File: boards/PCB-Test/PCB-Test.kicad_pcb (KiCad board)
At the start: 2 copper layers, 35.6 x 50.8 mm, 5 parts, among them U1 74HC137, U2 74HC137, U3 74HC137, U4 ATmega32-16A, U5 ATmega32-16M

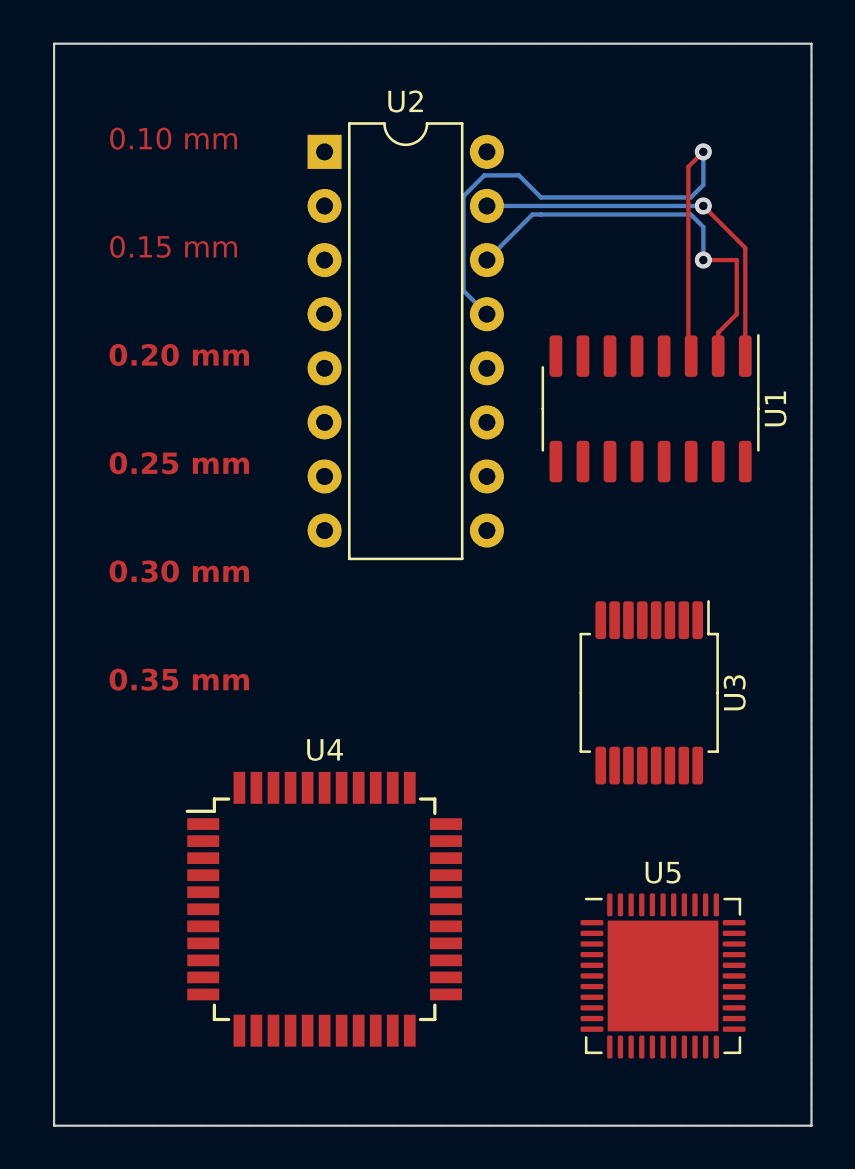
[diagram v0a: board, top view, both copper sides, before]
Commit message: Update PCB test board with different track sizes
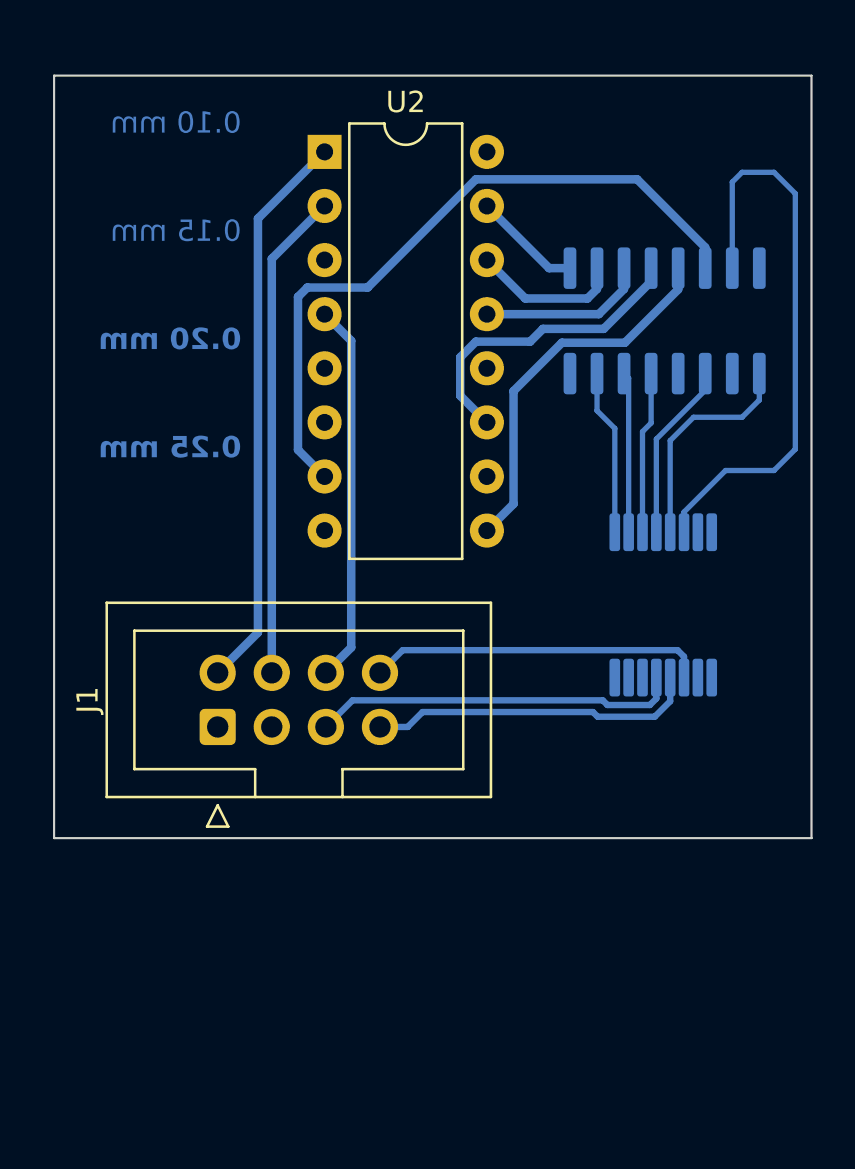
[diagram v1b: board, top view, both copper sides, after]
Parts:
- removed U4: ATmega32-16A, Package_QFP:TQFP-44_10x10mm_P0.8mm
- removed U5: ATmega32-16M, Package_DFN_QFN:QFN-44-1EP_7x7mm_P0.5mm_EP5.2x5.2mm
- added J1: Conn_02x04_Odd_Even, Connector_IDC:IDC-Header_2x04_P2.54mm_Vertical, F.Cu at (83.9, 93.0)
- U1, U3: moved to B.Cu
- moved U1 4.18 mm to (104.9, 74.0)
- moved U3 4.18 mm to (104.8, 87.3)
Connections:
- U2 pad 1: unconnected-(U2-A0-Pad1) -> Net-(J1-Pin_2)
- U2 pad 2: unconnected-(U2-A1-Pad2) -> Net-(J1-Pin_4)
- U2 pad 4: unconnected-(U2-~{LE}-Pad4) -> Net-(J1-Pin_6)
- U3 pad 11: unconnected-(U3-~{Y4}-Pad11) -> Net-(J1-Pin_8)
- U3 pad 12: unconnected-(U3-~{Y3}-Pad12) -> Net-(J1-Pin_7)
- U3 pad 13: unconnected-(U3-~{Y2}-Pad13) -> Net-(J1-Pin_5)
- U3 pad 14: unconnected-(U3-~{Y1}-Pad14) -> Net-(J1-Pin_3)
- U3 pad 15: unconnected-(U3-~{Y0}-Pad15) -> Net-(J1-Pin_1)
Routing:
- net Net-(U1-E2): track 0.00 -> 32.7 mm
- net Net-(U1-~{Y7}): track 0.00 -> 27.0 mm
- net Net-(J1-Pin_2): track 0.00 -> 26.5 mm
- net Net-(J1-Pin_4): track 0.00 -> 22.9 mm
- net Net-(U1-A2): track 29.8 -> 7.91 mm, vias 1 -> 0
- net Net-(J1-Pin_6): track 0.00 -> 17.9 mm
- net Net-(U1-~{E1}): track 0.00 -> 17.8 mm
- net Net-(J1-Pin_5): track 0.00 -> 17.2 mm
- net Net-(J1-Pin_8): track 0.00 -> 15.8 mm
- net Net-(J1-Pin_7): track 0.00 -> 15.4 mm
- net Net-(U1-~{LE}): track 0.00 -> 14.6 mm
- net Net-(U1-A0): track 18.0 -> 5.11 mm, vias 1 -> 0
- net Net-(U1-A1): track 19.3 -> 7.08 mm, vias 1 -> 0
- net Net-(U1-~{Y6}): track 0.00 -> 10.5 mm
- net Net-(U1-~{Y4}): track 0.00 -> 8.40 mm
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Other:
- board size 35.6 x 50.8 mm -> 35.6 x 35.8 mm
- board text removed: "0.30 mm"
- board text removed: "0.35 mm"

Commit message: Updated test PCB for milling, remove too small footprint
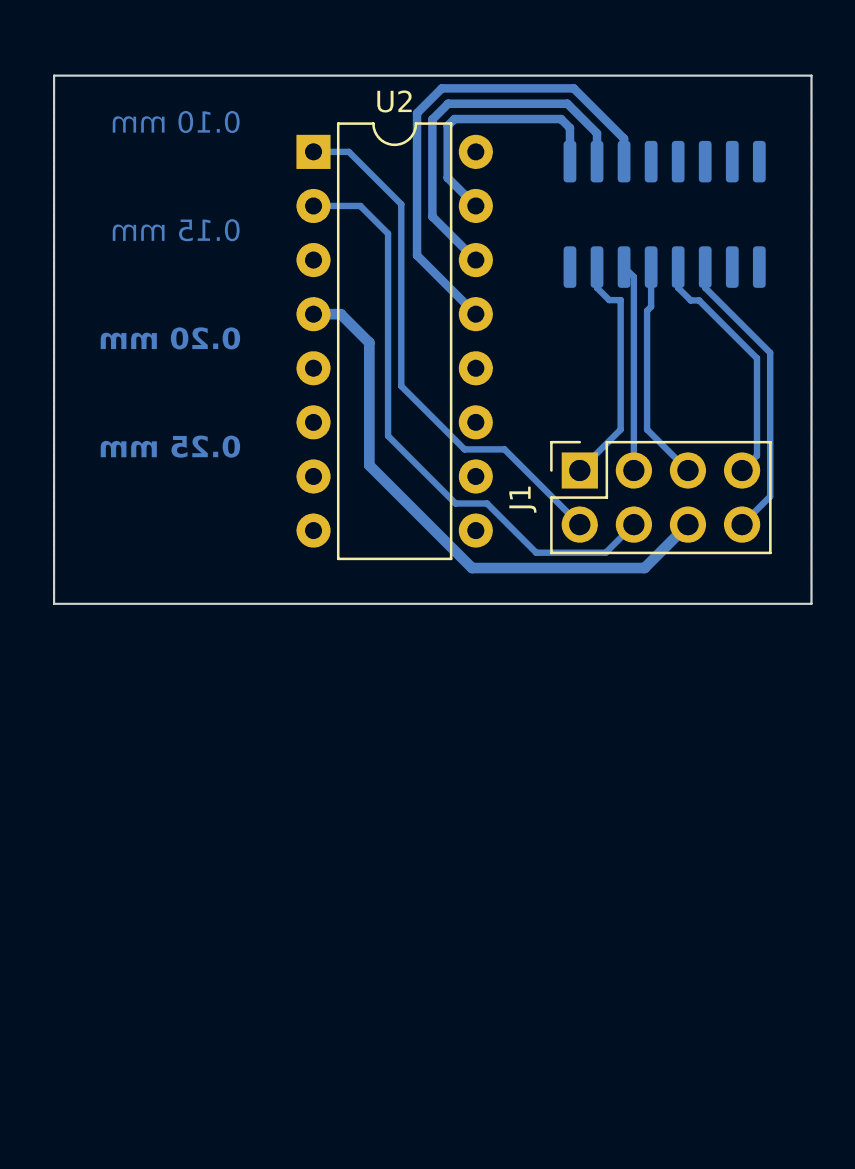
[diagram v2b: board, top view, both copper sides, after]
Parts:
- removed U3: 74HC137, Package_SO:SSOP-16_5.3x6.2mm_P0.65mm
- J1: value Conn_02x04_Odd_Even -> Conn; footprint Connector_IDC:IDC-Header_2x04_P2.54mm_Vertical -> Connector_PinSocket_2.54mm:PinSocket_2x04_P2.54mm_Vertical
- moved J1 20.8 mm to (100.9, 81.0)
- moved U1 5.00 mm to (104.9, 69.0)
- moved U2 0.52 mm to (88.4, 66.0)
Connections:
- U1 pad 11: Net-(U1-~{Y4}) -> Net-(J1-Pin_8)
- U1 pad 12: unconnected-(U1-~{Y3}-Pad12) -> Net-(J1-Pin_7)
- U1 pad 13: Net-(U1-~{Y2}) -> Net-(J1-Pin_5)
- U1 pad 14: Net-(U1-~{Y1}) -> Net-(J1-Pin_3)
- U1 pad 15: Net-(U1-~{Y0}) -> Net-(J1-Pin_1)
- U1 pad 7: Net-(U1-~{Y7}) -> unconnected-(U1-~{Y7}-Pad7)
- U1 pad 9: Net-(U1-~{Y6}) -> unconnected-(U1-~{Y6}-Pad9)
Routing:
- net Net-(U1-E2): track 32.7 -> 0.00 mm
- net Net-(U1-~{Y7}): track 27.0 -> 0.00 mm
- net Net-(U1-~{E1}): track 17.8 -> 0.00 mm
- net Net-(U1-A2): track 7.91 -> 23.6 mm
- net Net-(U1-~{LE}): track 14.6 -> 0.00 mm
- net Net-(J1-Pin_1): track 0.00 -> 11.1 mm
- net Net-(U1-~{Y6}): track 10.5 -> 0.00 mm
- net Net-(U1-A1): track 7.08 -> 17.4 mm
- net Net-(J1-Pin_3): track 0.00 -> 9.74 mm
- net Net-(J1-Pin_6): track 17.9 -> 26.7 mm
- net Net-(U1-~{Y4}): track 8.40 -> 0.00 mm
- net Net-(U1-~{Y0}): track 7.79 -> 0.00 mm
- net Net-(U1-~{Y2}): track 7.62 -> 0.00 mm
- net Net-(U1-~{Y1}): track 7.54 -> 0.00 mm
- net Net-(U1-A0): track 5.11 -> 11.9 mm
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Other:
- board size 35.6 x 35.8 mm -> 35.6 x 24.8 mm

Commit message: Added new PCB design rule templates for PCB milling
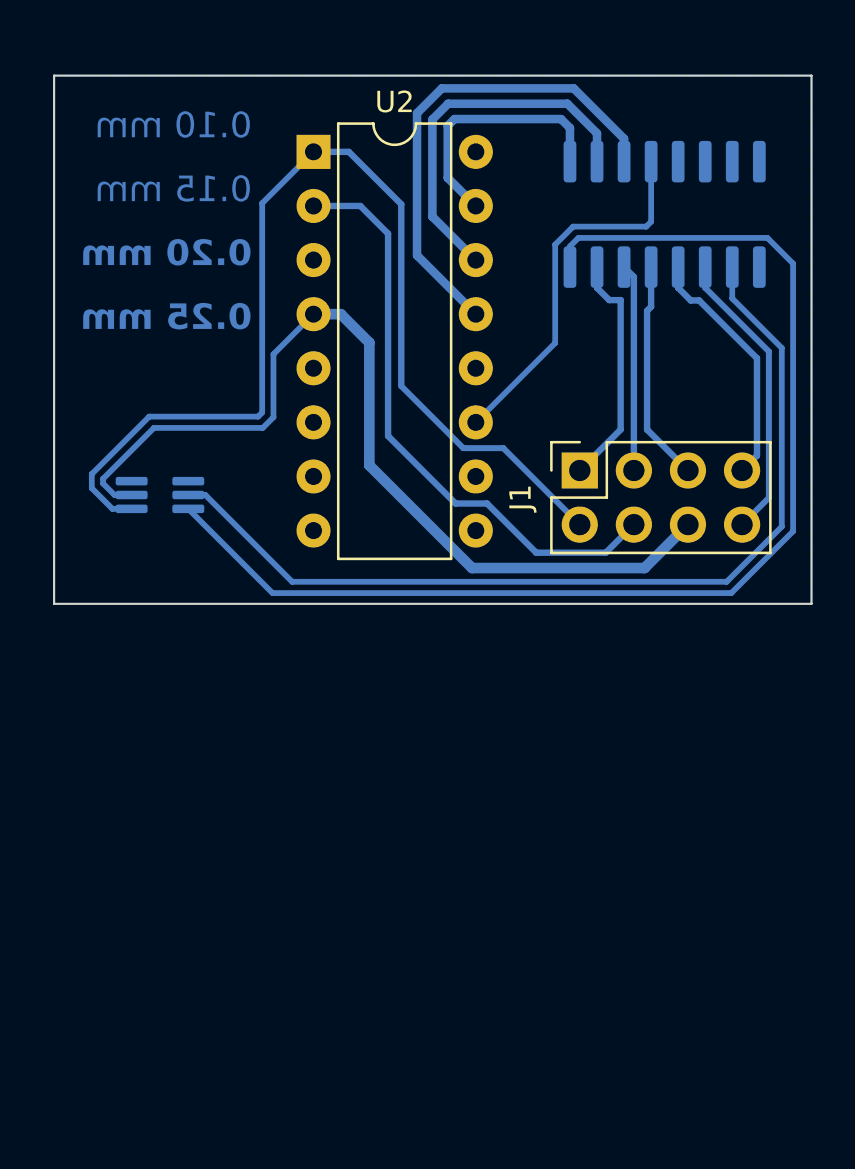
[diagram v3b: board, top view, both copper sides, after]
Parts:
- added U3: NCS210, Package_TO_SOT_SMD:SOT-363_SC-70-6_Handsoldering, B.Cu at (81.2, 82.2)
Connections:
- U1 pad 10: unconnected-(U1-~{Y5}-Pad10) -> Net-(U1-~{Y5})
- U1 pad 16: unconnected-(U1-VCC-Pad16) -> Net-(U1-VCC)
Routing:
- net Net-(U1-VCC): track 0.00 -> 55.9 mm
- net Net-(U1-~{Y5}): track 0.00 -> 43.8 mm
- net Net-(J1-Pin_2): track 24.7 -> 50.1 mm
- net Net-(U1-~{LE}): track 0.00 -> 17.7 mm
- net Net-(J1-Pin_6): track 26.7 -> 43.3 mm
